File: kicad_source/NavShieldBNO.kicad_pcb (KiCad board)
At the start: 2 copper layers, 36 x 23 mm, 40 parts, among them CN1 ARDUINO_MKR, CN2 CONN_01X04, CN3 CONN_01X04, U1 BNO085, U2 BMP388

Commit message: first draft of layout
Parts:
- moved R16 3.40 mm to (107.1, 161.2)
- moved R9 3.40 mm to (107.1, 164.6)
- moved R4 0.14 mm to (94.5, 160.6)
- moved R8 0.14 mm to (94.5, 162.3)
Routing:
- net GND: track 0.00 -> 129.0 mm, vias 0 -> 10
- net +3V3: track 0.00 -> 101.2 mm, vias 0 -> 2
- net /I2C_SDA: track 0.00 -> 51.7 mm, vias 0 -> 3
- net /I2C_SCL: track 0.00 -> 43.5 mm, vias 0 -> 2
- net /BNO085_INT: track 0.00 -> 31.1 mm, vias 0 -> 1
- net /RESET: track 0.00 -> 21.8 mm, vias 0 -> 2
- net /SPI_MISO: track 0.00 -> 20.7 mm, vias 0 -> 2
- net /BNO085_CS: track 0.00 -> 20.4 mm, vias 0 -> 1
- net /BMP388_INT: track 0.00 -> 18.8 mm, vias 0 -> 1
- net /SPI_MOSI: track 0.00 -> 17.7 mm, vias 0 -> 1
- net /SERIAL_RX: track 0.00 -> 14.6 mm
- net /SPI_SCK: track 0.00 -> 14.5 mm
- net /WAKE: track 0.00 -> 13.7 mm
- net /SERIAL_TX: track 0.00 -> 11.9 mm
- net /PS0: track 0.00 -> 7.51 mm
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- added copper zone on B.Cu, net GND
- added copper zone on F.Cu, net GND

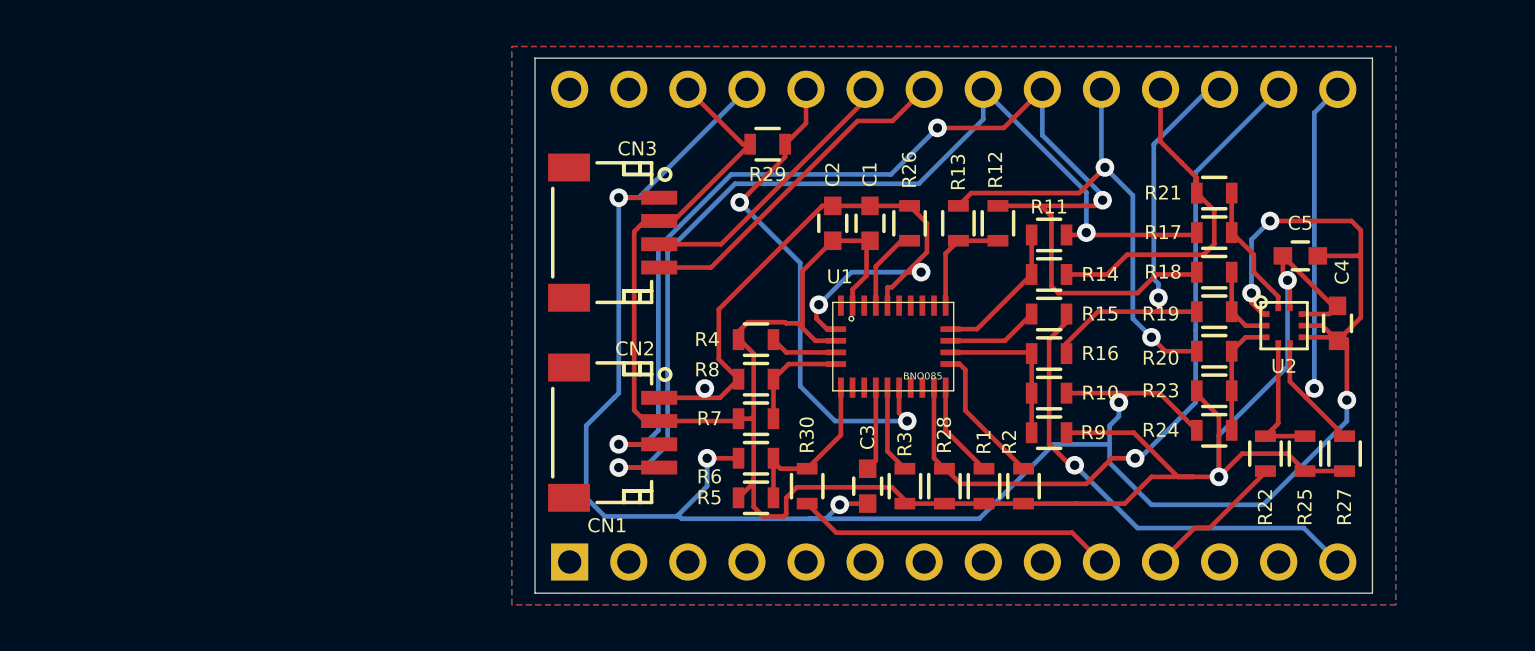
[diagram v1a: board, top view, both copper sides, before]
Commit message: made pcb bigger and added holes for Arduino MKR
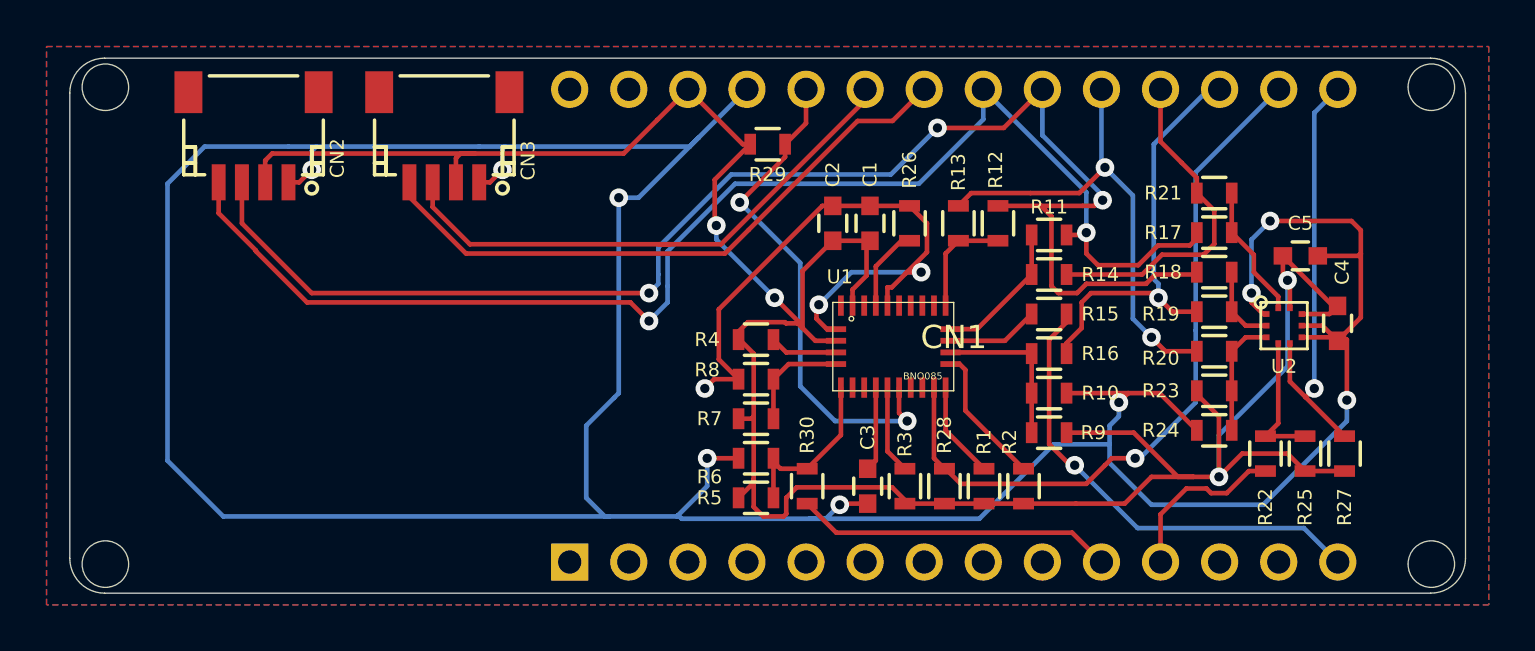
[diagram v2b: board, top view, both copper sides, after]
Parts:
- CN1: footprint MODULE_compute:ARDUINO_MKR -> MODULE_compute:ARDUINO_MKR_HOLES
- moved CN2 20.0 mm to (72.9, 151.9), turned to 180 degrees
- moved CN3 8.37 mm to (81.1, 151.9), turned to 180 degrees
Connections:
- net Net-(R10-Pad1) renamed /BNO085_H_MOSI
- net Net-(R11-Pad1) renamed /BNO085_H_SCK
- net Net-(R12-Pad1) renamed /BNO085_H_MISO
- net Net-(R15-Pad1) renamed /BNO085_H_CSN
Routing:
- net GND: track 129.0 -> 185.3 mm, vias 10 -> 12
- net /I2C_SCL: track 43.5 -> 57.8 mm
- net +3V3: track 101.2 -> 114.4 mm, vias 2 -> 4
- net /SERIAL_RX: track 14.6 -> 26.7 mm
- net /SERIAL_TX: track 11.9 -> 23.8 mm
- net /I2C_SDA: track 51.7 -> 62.8 mm
- net /BMP388_CS: track 6.16 -> 7.50 mm
- net /SPI_MOSI: track 17.7 -> 18.4 mm
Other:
- board size 36 x 23 mm -> 60 x 23 mm

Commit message: added second option for wake on A5, rearranged placement of option resistors and added description in silk screen
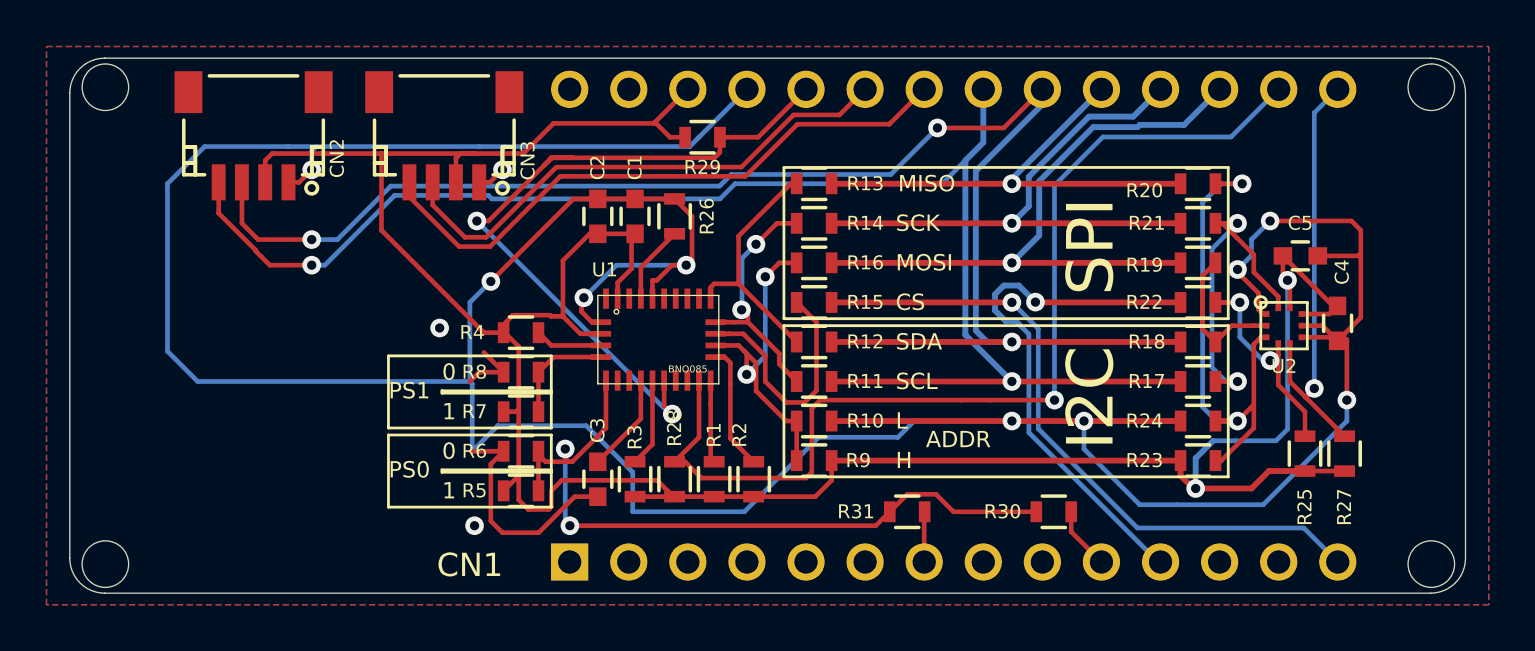
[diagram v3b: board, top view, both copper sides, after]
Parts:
- added R31: DNI, resistors:R_0603, F.Cu at (101.0, 168.0)
- moved R11 11.9 mm to (97.0, 162.4)
- moved R3 11.6 mm to (89.3, 166.6)
- moved C3 11.6 mm to (87.7, 166.6)
- moved R1 11.6 mm to (92.7, 166.6)
- moved R2 11.6 mm to (94.4, 166.6)
- moved R28 11.6 mm to (91.0, 166.6)
- moved R16 10.8 mm to (97.0, 157.3)
- moved R30 10.7 mm to (107.3, 168.0), turned to 0 degrees
- moved R14 10.3 mm to (97.0, 155.6)
- moved R9 10.2 mm to (97.0, 165.8)
- moved R10 10.2 mm to (97.0, 164.1)
- moved R15 10.1 mm to (97.0, 159.0)
- moved C1 10.1 mm to (89.3, 155.3)
- moved U1 10.1 mm to (90.3, 160.6)
- moved C2 10.1 mm to (87.7, 155.3)
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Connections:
- net /WAKE renamed /WAKE_1
- CN1 pad 7: (no net) -> /WAKE_2
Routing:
- net /PS0: track 7.51 -> 32.4 mm, vias 0 -> 2
- net /SDO: track 5.14 -> 23.1 mm, vias 0 -> 2
- net /BMP388_CS: track 7.50 -> 23.2 mm, vias 0 -> 1
- net GND: track 185.3 -> 171.9 mm
- net /BNO085_INT: track 31.1 -> 44.1 mm
- net /WAKE_1: track 13.7 -> 2.70 mm
- net /SPI_SCK: track 14.5 -> 24.5 mm, vias 0 -> 1
- net /SPI_MOSI: track 18.4 -> 28.4 mm
- net /RESET: track 21.8 -> 31.7 mm
- net /SCK: track 5.77 -> 15.1 mm, vias 0 -> 2
- net /BNO085_CS: track 20.4 -> 28.9 mm
- net /BNO085_H_MOSI: track 6.91 -> 14.4 mm, vias 0 -> 2
- net /I2C_SCL: track 57.8 -> 65.1 mm
- net /BNO085_H_CSN: track 3.96 -> 10.6 mm
- net /BNO085_H_MISO: track 4.72 -> 10.8 mm
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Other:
- board text added: "0"
- board text added: "1"
- board text added: "ADDR"
- board text added: "CS"
- board text added: "H"
- board text added: "I2C"
- board text added: "L"
- board text added: "MISO"
- board text added: "MOSI"
- board text added: "PS0"
- board text added: "PS1"
- board text added: "SCK"
- board text added: "SCL"
- board text added: "SDA"
- board text added: "SPI"

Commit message: added option for 32 kHz crystal, updated images and pdf
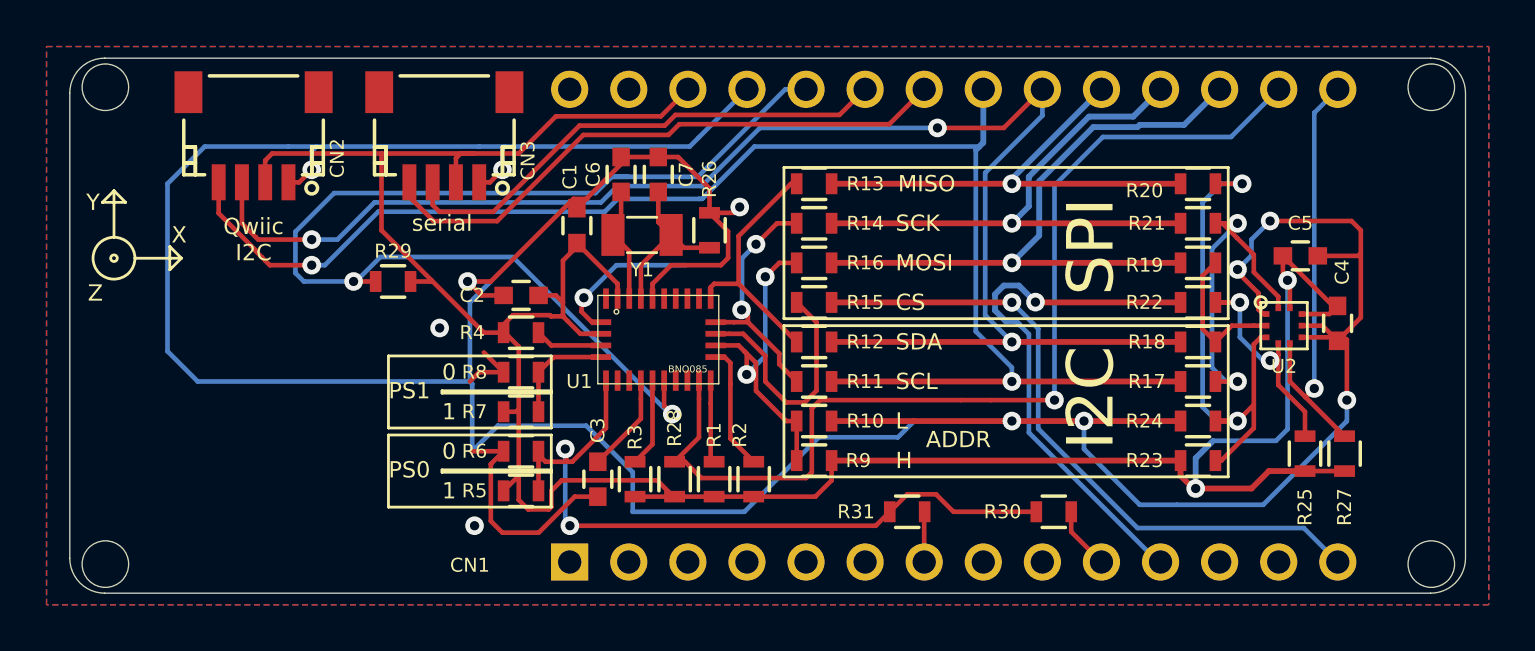
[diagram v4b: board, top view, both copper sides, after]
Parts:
- added C6: 22pF, capacitors:C_0603, F.Cu at (88.7, 153.5)
- added C7: 22pF, capacitors:C_0603, F.Cu at (90.3, 153.5)
- added Y1: DNI, crystals:Crystal_SMD_3.2x1.5mm_2Pad, F.Cu at (89.6, 156.1)
- moved R29 14.7 mm to (78.9, 158.1), turned to 180 degrees
- moved C2 4.74 mm to (84.4, 158.7), turned to 180 degrees
- moved C1 2.53 mm to (86.8, 155.7)
- moved R26 1.62 mm to (92.5, 155.9)
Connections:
- U1 pad 27: (no net) -> /XIN32
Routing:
- net /RESET: track 31.7 -> 49.0 mm
- net GND: track 171.9 -> 181.1 mm
- net /XIN32: track 0.00 -> 5.02 mm
- net /CLKSEL1: track 3.74 -> 7.58 mm
- net +3V3: track 117.9 -> 115.9 mm
- net /I2C_SDA: track 67.4 -> 66.5 mm
- net /SERIAL_TX: track 22.8 -> 21.9 mm
- net /SERIAL_RX: track 26.4 -> 25.5 mm
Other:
- board text added: "Qwiic I2C"
- board text added: "X"
- board text added: "Y"
- board text added: "Z"
- board text added: "serial"

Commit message: added BME280/BMP280
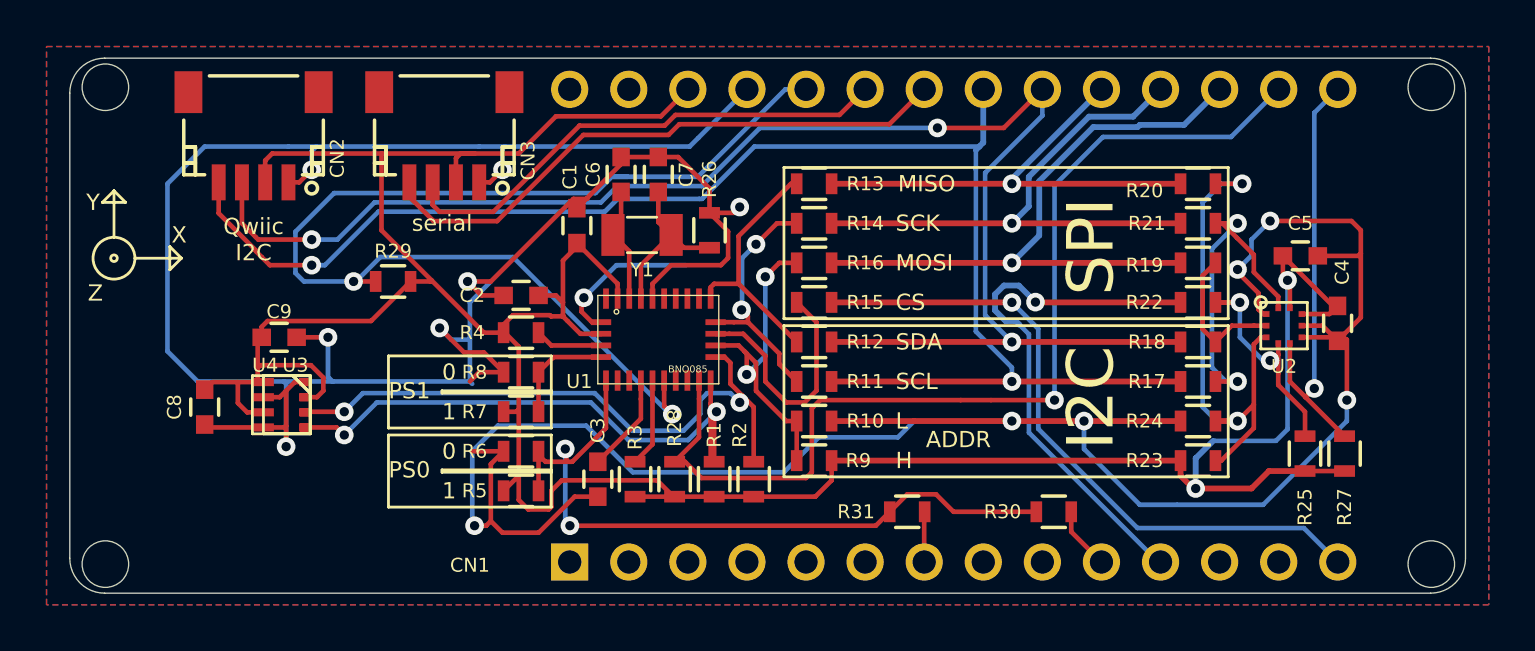
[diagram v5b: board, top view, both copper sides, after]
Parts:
- added C8: 100nF, capacitors:C_0603, F.Cu at (70.8, 163.5)
- added C9: 100nF, capacitors:C_0603, F.Cu at (74.0, 160.5)
- added U3: BMP280, IC_sensor:BMP280, F.Cu at (74.3, 163.4)
- added U4: BME280, IC_sensor:BME280, F.Cu at (74.1, 163.4)
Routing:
- net /ENV_SCL: track 3.55 -> 25.3 mm, vias 0 -> 2
- net GND: track 181.1 -> 202.4 mm, vias 12 -> 14
- net /ENV_SDA: track 5.41 -> 26.6 mm, vias 0 -> 2
- net +3V3: track 115.9 -> 135.3 mm

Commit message: added Vishay VCNL4040
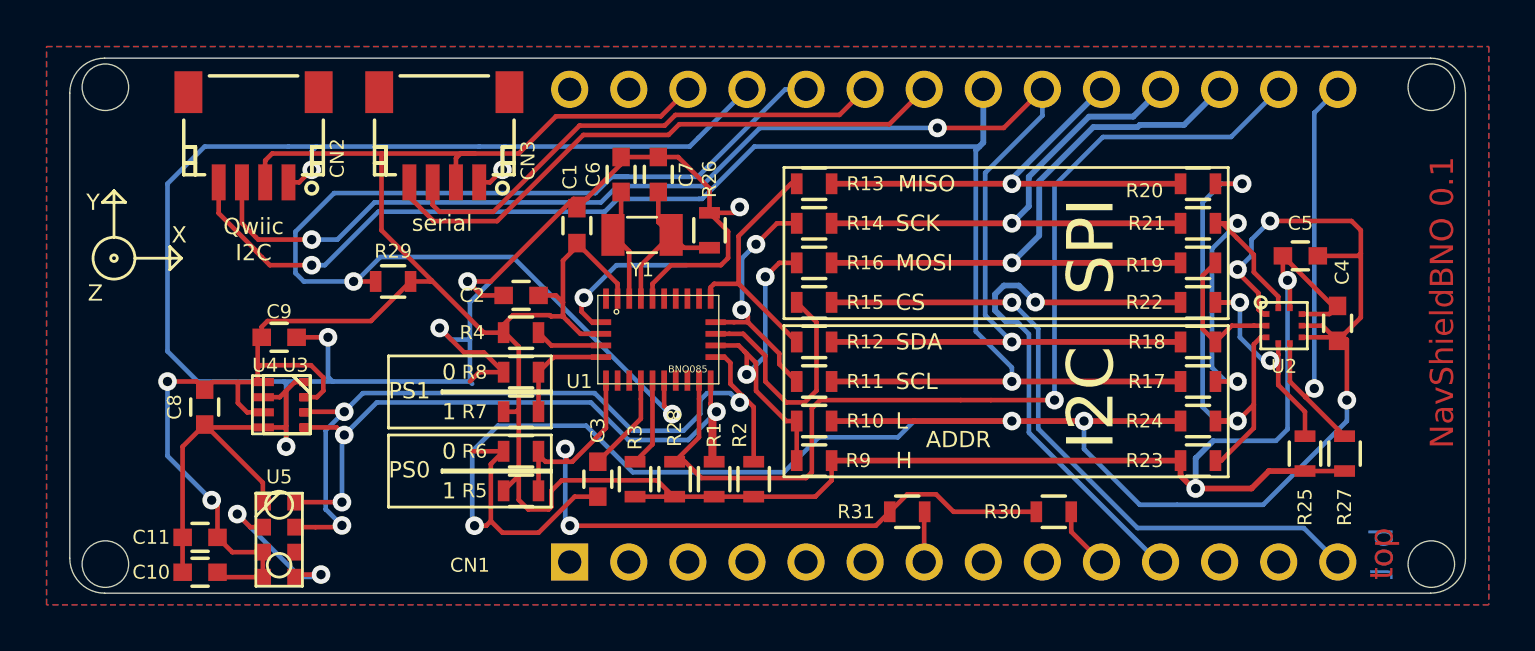
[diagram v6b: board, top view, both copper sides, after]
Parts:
- added C10: 100nF, capacitors:C_0603, F.Cu at (70.6, 170.6)
- added C11: 100nF, capacitors:C_0603, F.Cu at (70.6, 169.1)
- added U5: VCNL4040, IC_sensor:VCNL4040, F.Cu at (74.0, 169.2)
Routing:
- net +3V3: track 135.3 -> 150.0 mm, vias 2 -> 4
- net GND: track 202.4 -> 213.5 mm
- net /ENV_SDA: track 26.6 -> 34.2 mm, vias 2 -> 3
- net Net-(U5-Pad2): track 0.00 -> 7.24 mm, vias 0 -> 2
- net /ENV_SCL: track 25.3 -> 30.2 mm, vias 2 -> 3
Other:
- board text added: "NavShieldBNO 0.1"
- board text added: "bot"
- board text added: "top"

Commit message: added logo, updated images and pdf
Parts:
- added L1: Label, labels:generationmake_small_solder, F.Cu at (124.1, 157.8)

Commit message: updated layout, made DRC, updated silk screen
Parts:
- added L2: Label, labels:generationmake_logo, B.Cu at (98.9, 160.7)
- added W1: TEST_1P, wire_pads:SolderWirePad_single_1mmSMD, F.Cu at (77.9, 164.9)
- added W2: TEST_1P, wire_pads:SolderWirePad_single_1mmSMD, F.Cu at (77.9, 163.5)
- added W3: TEST_1P, wire_pads:SolderWirePad_single_1mmSMD, F.Cu at (104.3, 162.4)
- added W4: TEST_1P, wire_pads:SolderWirePad_single_1mmSMD, F.Cu at (104.3, 160.7)
- added W5: TEST_1P, wire_pads:SolderWirePad_single_1mmSMD, F.Cu at (104.3, 153.9)
- added W6: TEST_1P, wire_pads:SolderWirePad_single_1mmSMD, F.Cu at (104.3, 155.6)
- added W7: TEST_1P, wire_pads:SolderWirePad_single_1mmSMD, F.Cu at (104.3, 157.3)
- added W8: TEST_1P, wire_pads:SolderWirePad_single_1mmSMD, F.Cu at (76.0, 169.5)
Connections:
- U5 pad 6: (no net) -> /INT
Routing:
- net +3V3: track 150.0 -> 172.1 mm, vias 4 -> 6
- net GND: track 213.5 -> 211.7 mm, vias 14 -> 29
- net /PS0: track 32.4 -> 33.9 mm
- net /INT: track 0.00 -> 1.40 mm
- net /RESET: track 49.0 -> 47.8 mm
- net /SDO: track 23.1 -> 22.1 mm
- net /ENV_SCL: track 30.2 -> 31.1 mm
- net /BMP388_INT: track 18.8 -> 19.3 mm
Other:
- board text added: "NavShieldBNO"
- board text added: "find more information on https://github.com/generationmake/NavShieldBNO"
- board text added: "navigation shield with Bosch BNO085 and BMP388"
